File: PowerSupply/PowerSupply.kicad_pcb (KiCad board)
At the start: 2 copper layers, 40.3 x 22.9 mm, 29 parts, among them IC1 MCP73832T-2DCI_OT, J1 Conn_01x04_Male, J2 Barrel_Jack, Q1 DMP2045U-7, Q2 DMP2045U-7, U1 AP3012, U2 AP3012

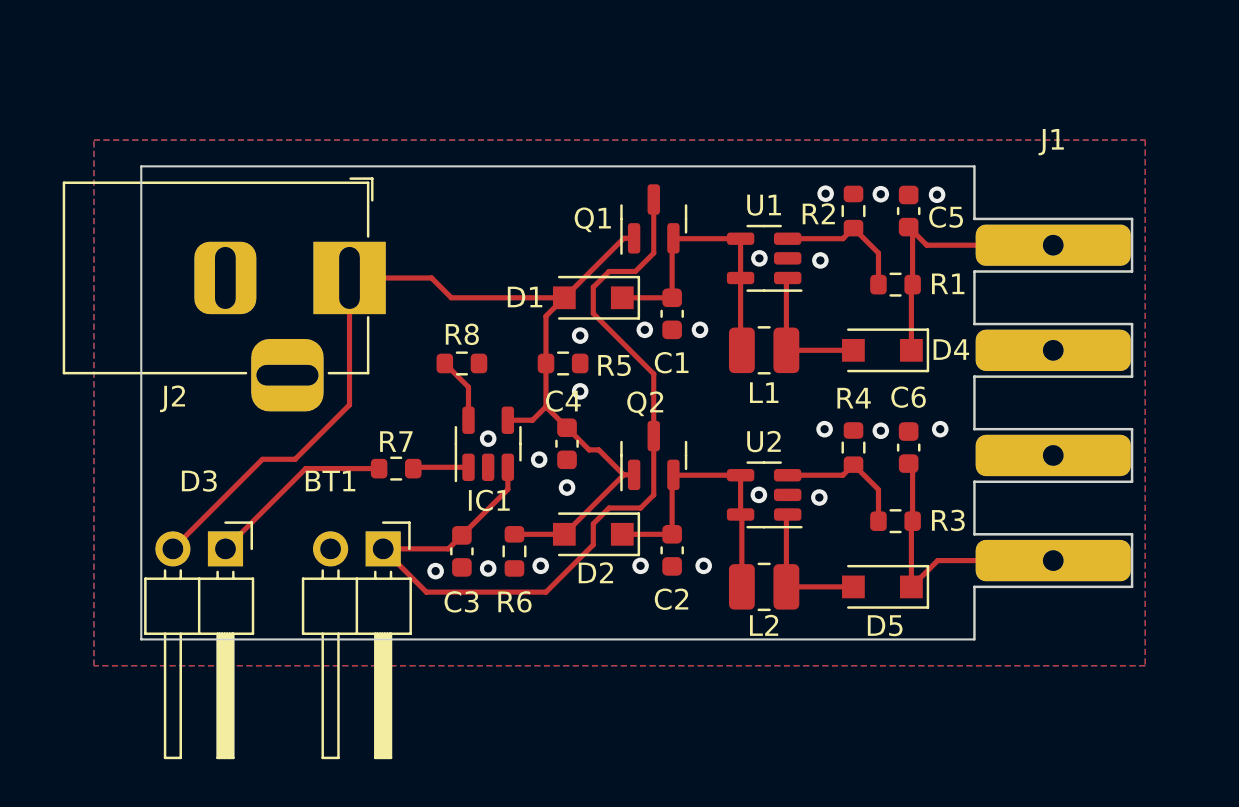
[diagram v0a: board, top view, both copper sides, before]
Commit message: Added power switch
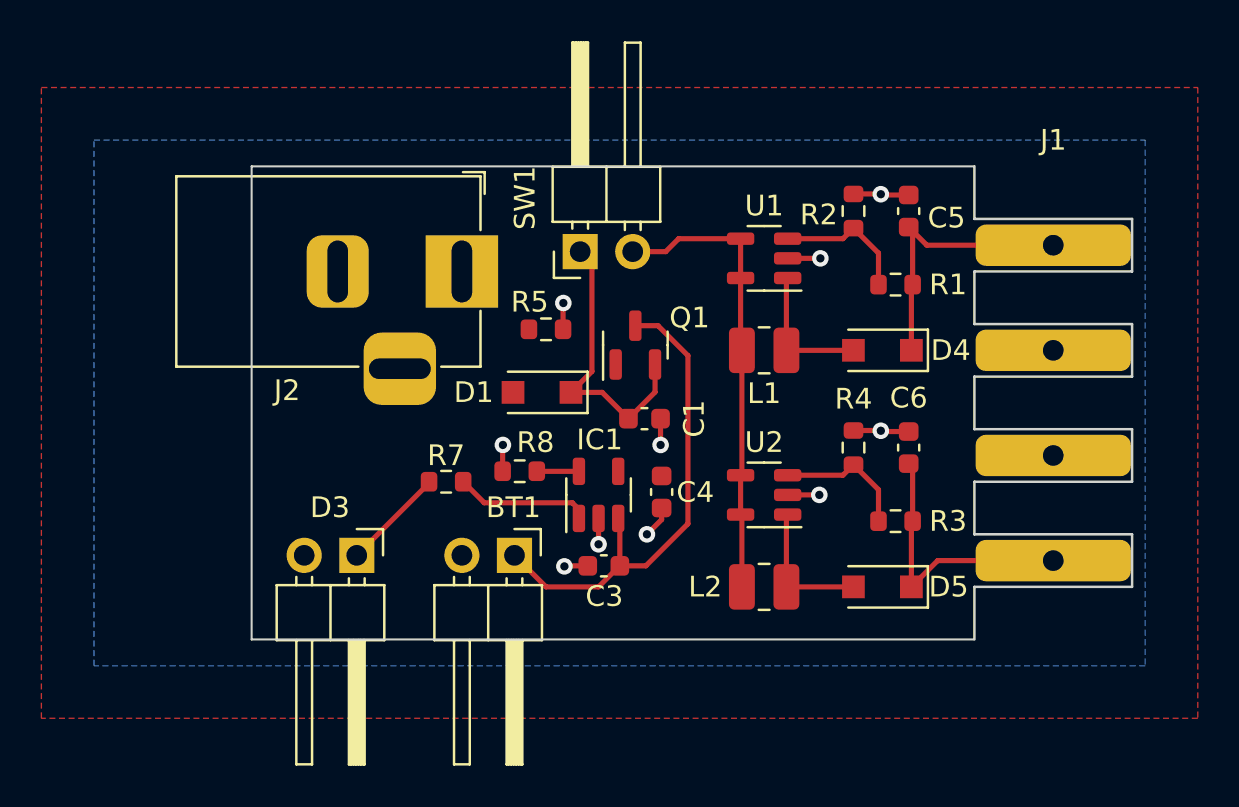
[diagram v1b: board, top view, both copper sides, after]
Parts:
- removed C2: 1uF, Capacitor_SMD:C_0603_1608Metric
- removed D2: 2SS100L, Diode_SMD:D_SOD-123F
- removed Q2: DMP2045U-7, Package_TO_SOT_SMD:SOT-23
- removed R6: 100k, Resistor_SMD:R_0603_1608Metric
- added SW1: SW_SPST, Connector_PinHeader_2.54mm:PinHeader_1x02_P2.54mm_Horizontal, F.Cu at (155.6, 68.9)
- moved C3 6.89 mm to (156.7, 84.1), turned to 0 degrees
- moved BT1 6.35 mm to (152.4, 83.6)
- moved D3 6.35 mm to (144.8, 83.6)
- moved Q1 6.16 mm to (158.2, 73.4)
- moved R8 5.91 mm to (152.7, 79.5), turned to 0 degrees
- moved IC1 5.88 mm to (156.5, 80.6)
- moved J2 5.44 mm to (149.9, 69.8)
- moved C1 5.24 mm to (158.7, 77.0), turned to 0 degrees
- moved D1 5.20 mm to (153.7, 75.7)
- moved C4 5.13 mm to (159.5, 80.5)
- moved R7 2.50 mm to (149.1, 80.0)
- moved R5 1.85 mm to (153.9, 72.6)
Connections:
- L1 pad 1: Net-(C1-Pad1) -> Net-(L2-Pad1)
- L2 pad 1: Net-(C2-Pad1) -> Net-(L2-Pad1)
- U1 pad 4: Net-(C1-Pad1) -> Net-(L2-Pad1)
- U1 pad 5: Net-(C1-Pad1) -> Net-(L2-Pad1)
- U2 pad 4: Net-(C2-Pad1) -> Net-(L2-Pad1)
- U2 pad 5: Net-(C2-Pad1) -> Net-(L2-Pad1)
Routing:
- net +5V: track 52.7 -> 0.00 mm
- net Net-(L2-Pad1): track 0.00 -> 22.4 mm
- net +BATT: track 42.2 -> 23.9 mm
- net GND: track 0.00 -> 16.3 mm, vias 22 -> 10
- net Net-(C2-Pad1): track 14.0 -> 0.00 mm
- net Net-(D3-Pad1): track 9.03 -> 5.00 mm
- net Net-(IC1-Pad1): track 2.70 -> 6.58 mm
- net Net-(IC1-Pad5): track 3.22 -> 2.04 mm
- added copper zone on F.Cu, net +5V
- removed copper zone on F.Cu, net GND
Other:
- board size 40.3 x 22.9 mm -> 34.9 x 22.9 mm

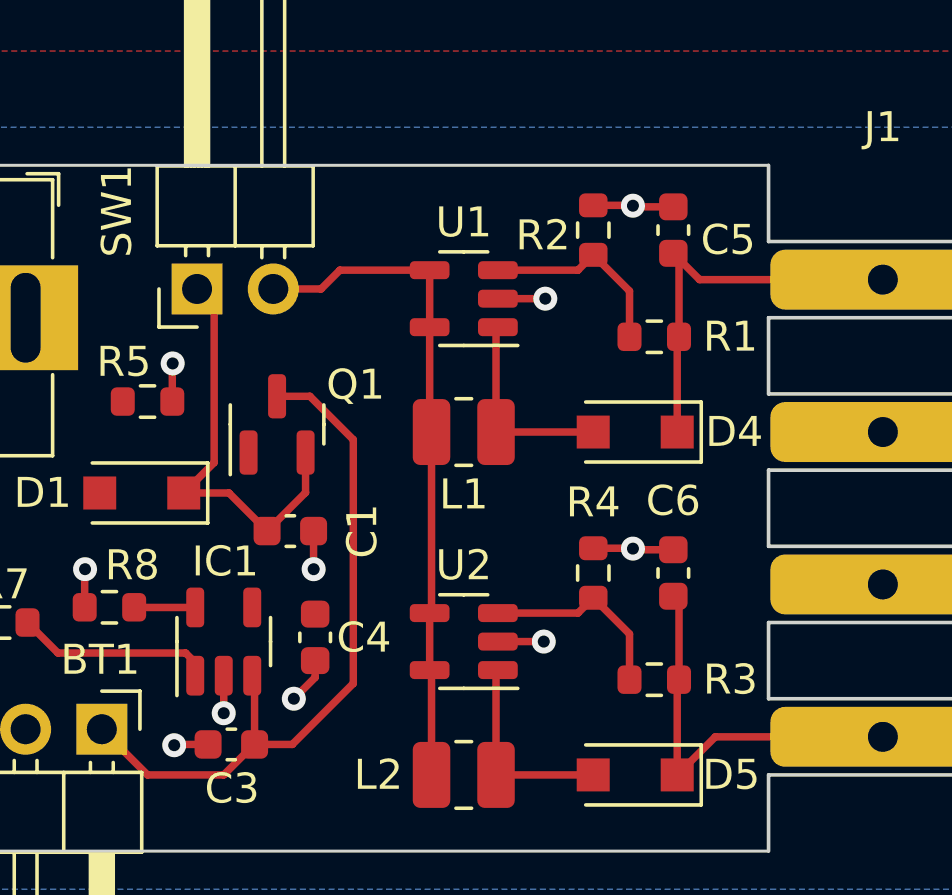
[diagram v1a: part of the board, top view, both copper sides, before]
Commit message: Moved capacitors for regulators to other side of power switch.
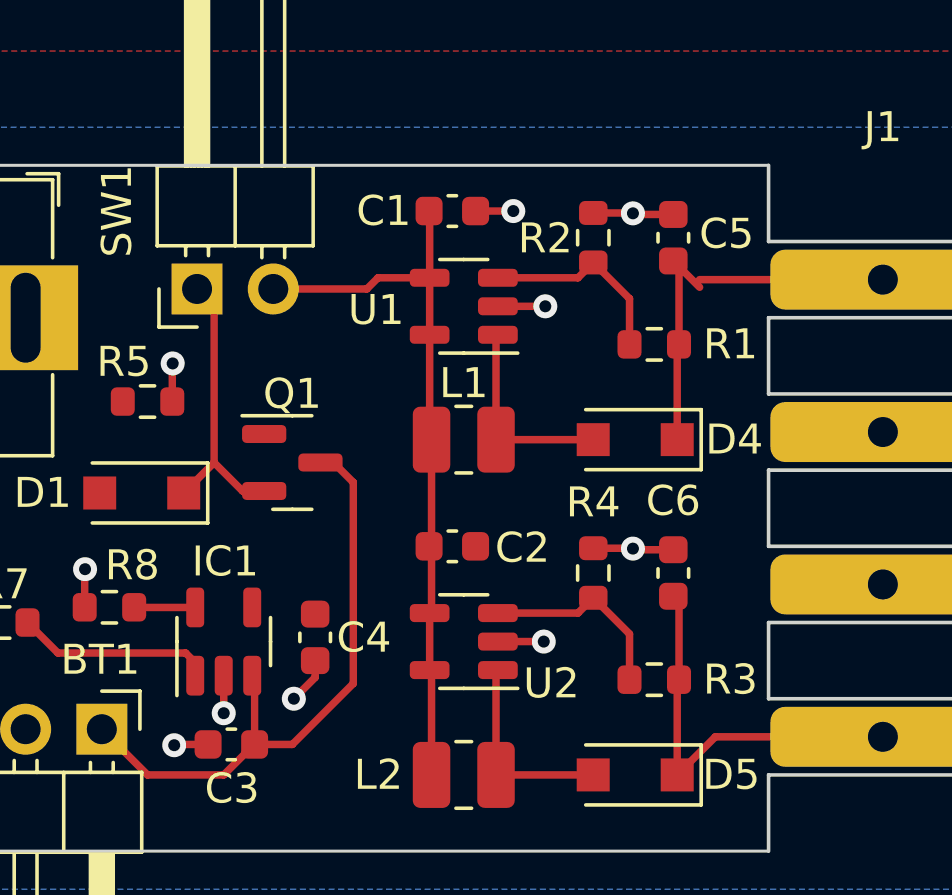
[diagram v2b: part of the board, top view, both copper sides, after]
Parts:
- added C2: 1uF, Capacitor_SMD:C_0603_1608Metric, F.Cu at (164.1, 77.5)
- moved C1 12.0 mm to (164.1, 66.3)
- moved Q1 1.37 mm to (158.8, 74.7), turned to 0 degrees
- moved C5 0.25 mm to (171.4, 67.2)
- moved D4 0.25 mm to (170.2, 73.9)
- moved L1 0.25 mm to (164.5, 73.9)
- moved R1 0.25 mm to (170.8, 70.7)
- moved R2 0.25 mm to (168.8, 67.2)
- moved U1 0.25 mm to (164.5, 69.5)
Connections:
- C1 pad 1: Net-(C1-Pad1) -> Net-(L1-Pad1)
- D1 pad 1: Net-(C1-Pad1) -> Net-(D1-Pad1)
- L1 pad 1: Net-(L2-Pad1) -> Net-(L1-Pad1)
- L2 pad 1: Net-(L2-Pad1) -> Net-(L1-Pad1)
- Q1 pad 2: Net-(C1-Pad1) -> Net-(D1-Pad1)
- SW1 pad 1: Net-(C1-Pad1) -> Net-(D1-Pad1)
- SW1 pad 2: Net-(L2-Pad1) -> Net-(L1-Pad1)
- U1 pad 4: Net-(L2-Pad1) -> Net-(L1-Pad1)
- U1 pad 5: Net-(L2-Pad1) -> Net-(L1-Pad1)
- U2 pad 4: Net-(L2-Pad1) -> Net-(L1-Pad1)
- U2 pad 5: Net-(L2-Pad1) -> Net-(L1-Pad1)
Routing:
- net Net-(L1-Pad1): track 0.00 -> 24.5 mm
- net Net-(L2-Pad1): track 22.4 -> 0.00 mm
- net Net-(C1-Pad1): track 13.9 -> 0.00 mm
- net Net-(D1-Pad1): track 0.00 -> 9.52 mm
- net +BATT: track 23.9 -> 20.7 mm
